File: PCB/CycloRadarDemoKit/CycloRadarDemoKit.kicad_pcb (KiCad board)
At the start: 2 copper layers, 110 x 110 mm, 89 parts, among them J201 ARJM11B1-009-AB-EW2, Q301 L8050QLT1G, Q302 L8050QLT1G, Q401 SI2309CDS, SW101 RESET, SW102 BOOT MODE, U101 ESP32-WROVER-E, U201 IP101GRI, U301 CP2102N-Axx-xQFN28, U401 INA3221, U402 RT8259, U403 TPS2121RUXR, U404 AP63205WU, U405 AP63203WU, Y201 25MHz

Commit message: MPU added, power managemennt updated
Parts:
- removed the C403 at (166.0, 61.5)
- removed the L403 at (162.4, 89.9)
- removed the R402 at (156.3, 62.6)
- removed R418: 0R, Resistor_SMD:R_0805_2012Metric
- added R201: 0R, Resistor_SMD:R_0805_2012Metric, F.Cu at (167.6, 132.5)
- added R308: 5.1K(1%), Resistor_SMD:R_0603_1608Metric, F.Cu at (117.4, 73.5)
- added R309: 5.1K(1%), Resistor_SMD:R_0603_1608Metric, F.Cu at (117.4, 76.0)
- added R414: 47k(1%), Resistor_SMD:R_0603_1608Metric, F.Cu at (172.4, 78.8)
- added U501: MPU-6050, Sensor_Motion:InvenSense_QFN-24_4x4mm_P0.5mm, F.Cu at (160.2, 134.2)
- added U502: LSM6DSM, Package_LGA:LGA-14_3x2.5mm_P0.5mm_LayoutBorder3x4y, F.Cu at (121.8, 50.1)
- added U503: D52MxxM8, RF_Module:Garmin_M8-35_9.8x14.0mm_Layout6x6_P1.5mm, F.Cu at (111.5, 59.8)
- R211: renamed from R210; value 120 -> 270
- R213: renamed from R212; value 100 -> 220
- moved U201 57.6 mm to (105.8, 71.1)
- moved U401 3.49 mm to (188.9, 72.5)
- renumbered C303 to C301, C304 to C302, C301 to C303, C302 to C304, R104 to R107, R105 to R108, R106 to R109, R209 to R210, R213 to R214
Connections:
- net /MAC_TXD(0) renamed /MAC_TXD0
- net /MAC_TXD(1) renamed /MAC_TXD1
- net /USB interface/DTR renamed /USB + LED/DTR
- net /USB interface/RTS renamed /USB + LED/RTS
- net /USB interface/RXD renamed /USB + LED/RXD
- net /USB interface/TXD renamed /USB + LED/TXD
- C401 pad 1: Net-(U401-IN+1) -> Net-(U401-PV)
- C401 pad 2: Net-(U401-IN-1) -> Net-(U401-CRITICAL)
- C402 pad 1: Net-(U401-IN-2) -> Net-(U401-A0)
- C402 pad 2: Net-(U401-IN+2) -> Net-(U401-TC)
- C413 pad 1: /Power management/5V_MUX -> +5V
- D102 pad 3: /IO0 -> /MAC_CLK
- D304 pad 4: /USB interface/LED_DIN -> /LED_DIN
- R109 pad 2: unconnected-(R106-Pad2) -> /GPIO2
- R413 pad 2: +5V -> Net-(D403-A)
- U101 pad 26: unconnected-(U101-ADC2_CH0/GPIO4-Pad26) -> /LED_DIN
- U101 pad 4: unconnected-(U101-SENSOR_VP/GPIO36/ADC1_CH0-Pad4) -> /Photo_res
- U101 pad 5: unconnected-(U101-SENSOR_VN/GPIO39/ADC1_CH3-Pad5) -> /IMU_INT
- U101 pad 6: unconnected-(U101-GPIO34/ADC1_CH6-Pad6) -> SDA
- U101 pad 7: unconnected-(U101-GPIO35/ADC1_CH7-Pad7) -> SCL
- U101 pad 8: unconnected-(U101-32K_XP/GPIO32/ADC1_CH4-Pad8) -> /PMIC_INT
- U101 pad 9: unconnected-(U101-32K_XN/GPIO33/ADC1_CH5-Pad9) -> /12V_DIS
- U401 pad 1: Net-(U401-IN-2) -> GND
- U401 pad 10: /Power management/PMIC_PV -> Net-(U401-PV)
- U401 pad 11: Net-(U401-IN-1) -> unconnected-(U401-IN-1-Pad11)
- U401 pad 12: Net-(U401-IN+1) -> /PMIC_INT
- U401 pad 13: unconnected-(U401-TC-Pad13) -> Net-(U401-TC)
- U401 pad 14: Net-(U401-IN-2) -> unconnected-(U401-IN-2-Pad14)
- U401 pad 15: Net-(U401-IN+2) -> unconnected-(U401-IN+2-Pad15)
- U401 pad 2: unconnected-(U401-IN+3-Pad2) -> SCL
- U401 pad 5: GND -> Net-(U401-A0)
- U401 pad 6: SCL -> unconnected-(U401-SCL-Pad6)
- U401 pad 7: SDA -> unconnected-(U401-SDA-Pad7)
- U401 pad 9: unconnected-(U401-CRITICAL-Pad9) -> Net-(U401-CRITICAL)
- U402 pad 4: /Power management/12V_EN -> /12V_DIS
- U403 pad 1: /Power management/5V_MUX -> +5V
- U403 pad 6: +5V -> Net-(D403-A)
- U403 pad 7: +5V -> Net-(D403-A)
- U403 pad 8: /Power management/5V_MUX -> +5V
- U405 pad 2: /Power management/5V_MUX -> +5V
- U405 pad 3: /Power management/5V_MUX -> +5V

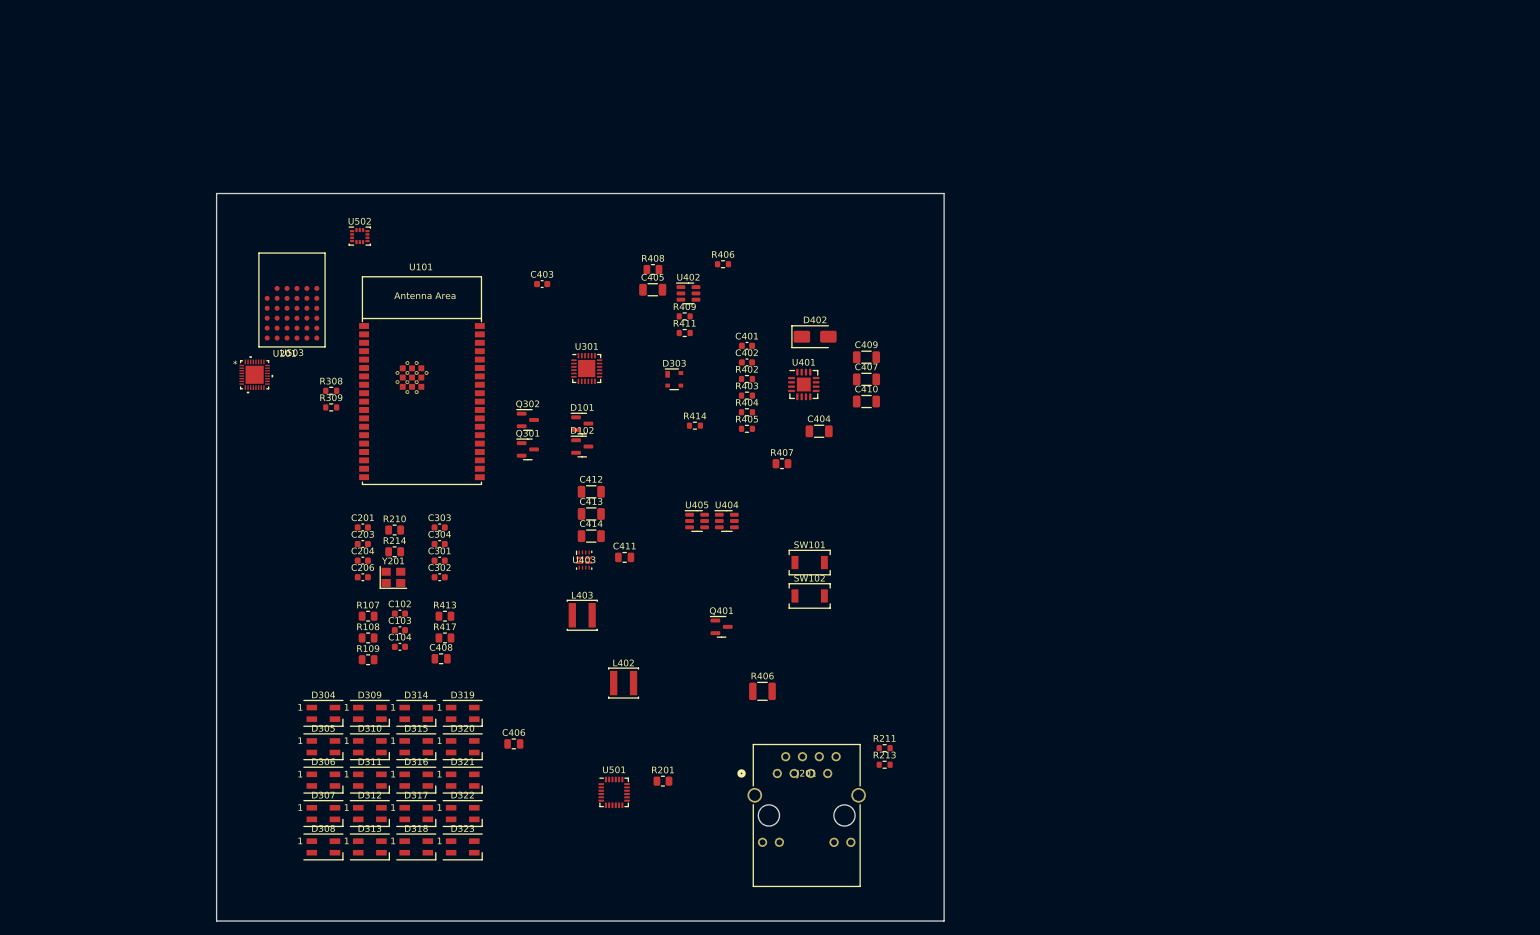
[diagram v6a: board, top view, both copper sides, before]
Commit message: added buzzer and pins for Radar
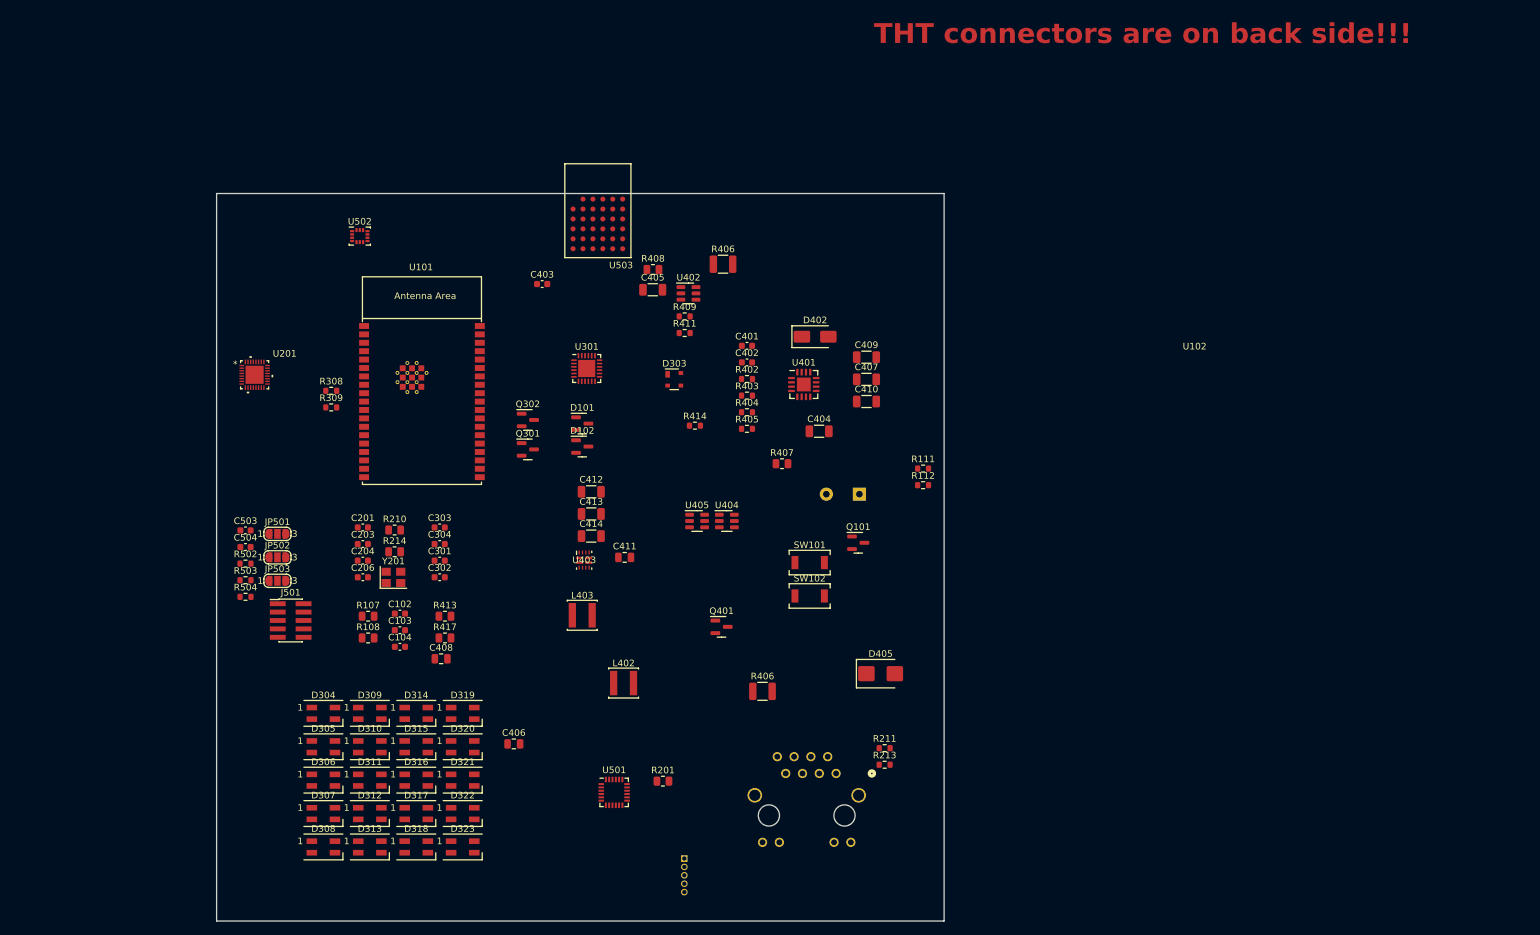
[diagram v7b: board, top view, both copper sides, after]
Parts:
- removed R109: 0R, Resistor_SMD:R_0805_2012Metric
- added BZ101: Buzzer, Buzzer_Beeper:Buzzer_D9mm_P5mm, B.Cu at (197.3, 89.1)
- added C503: 100nF/10V, Capacitor_SMD:C_0603_1608Metric, F.Cu at (104.5, 94.6)
- added C504: 100nF/10V, Capacitor_SMD:C_0603_1608Metric, F.Cu at (104.5, 97.1)
- added D405: SMBJ20A, Diode_SMD:D_SMB, F.Cu at (200.5, 116.2)
- added J101: I2C conn, Connector_PinHeader_1.27mm:PinHeader_1x05_P1.27mm_Vertical, B.Cu at (170.8, 144.2)
- added J501: JTAG, Connector_PinHeader_1.27mm:PinHeader_2x05_P1.27mm_Vertical_SMD, F.Cu at (111.3, 108.2)
- added JP501: BR1, Jumper:SolderJumper-3_P1.3mm_Open_RoundedPad1.0x1.5mm_NumberLabels, F.Cu at (109.3, 95.1)
- added JP502: BR2, Jumper:SolderJumper-3_P1.3mm_Open_RoundedPad1.0x1.5mm_NumberLabels, F.Cu at (109.3, 98.7)
- added JP503: BR3, Jumper:SolderJumper-3_P1.3mm_Open_RoundedPad1.0x1.5mm_NumberLabels, F.Cu at (109.3, 102.2)
- added Q101: L8050QLT1G, Package_TO_SOT_SMD:SOT-23, F.Cu at (197.1, 96.5)
- added R111: ???, Resistor_SMD:R_0603_1608Metric, F.Cu at (206.9, 85.2)
- added R112: 10K(5%), Resistor_SMD:R_0603_1608Metric, F.Cu at (206.9, 87.8)
- added R502: 0R, Resistor_SMD:R_0603_1608Metric, F.Cu at (104.5, 99.6)
- added R503: 0R, Resistor_SMD:R_0603_1608Metric, F.Cu at (104.5, 102.1)
- added R504: 0R, Resistor_SMD:R_0603_1608Metric, F.Cu at (104.5, 104.6)
- added U102: RADAR POGO pins, alps_modules:ALPS Generic Radar 5, F.Cu at (217.5, 100.5)
- J201: moved to B.Cu
- R406: value ??? -> 0.16R(5%); footprint Resistor_SMD:R_0603_1608Metric -> Resistor_SMD:R_1210_3225Metric
- moved U503 48.2 mm to (157.8, 46.2)
- turned J201 to 180 degrees
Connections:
- net Net-(U503-VCC-PadB5) renamed /IMU + ANT/VCC
- C401 pad 1: Net-(U401-PV) -> Net-(U401-IN+1)
- C401 pad 2: Net-(U401-CRITICAL) -> Net-(U401-IN-1)
- C402 pad 1: Net-(U401-A0) -> Net-(U401-IN-2)
- C402 pad 2: Net-(U401-TC) -> Net-(U401-IN+2)
- R406 pad 1: Net-(D402-K) -> Net-(Q401-S)
- R406 pad 2: GND -> Net-(R403-Pad2)
- U101 pad 13: /TMS -> /RXD1
- U101 pad 14: /TDI -> /Radar_GPIO
- U101 pad 16: /TCK -> /RTS1
- U101 pad 23: /TDO -> /TXD1
- U101 pad 24: /GPIO2 -> /Buzzer
- U401 pad 1: GND -> Net-(U401-IN-2)
- U401 pad 10: Net-(U401-PV) -> /PMIC_INT
- U401 pad 11: unconnected-(U401-IN-1-Pad11) -> Net-(U401-IN-1)
- U401 pad 12: /PMIC_INT -> Net-(U401-IN+1)
- U401 pad 13: Net-(U401-TC) -> unconnected-(U401-TC-Pad13)
- U401 pad 14: unconnected-(U401-IN-2-Pad14) -> Net-(U401-IN-2)
- U401 pad 15: unconnected-(U401-IN+2-Pad15) -> Net-(U401-IN+2)
- U401 pad 2: SCL -> unconnected-(U401-IN+3-Pad2)
- U401 pad 5: Net-(U401-A0) -> GND
- U401 pad 6: unconnected-(U401-SCL-Pad6) -> SCL
- U401 pad 7: unconnected-(U401-SDA-Pad7) -> SDA
- U401 pad 9: Net-(U401-CRITICAL) -> unconnected-(U401-CRITICAL-Pad9)
- U503 pad A2: Net-(U503-VSS-PadA2) -> GND
- U503 pad A3: Net-(U503-VSS-PadA2) -> GND
- U503 pad A4: Net-(U503-VSS-PadA2) -> GND
- U503 pad A5: Net-(U503-VSS-PadA2) -> GND
- U503 pad A6: Net-(U503-VSS-PadA2) -> GND
- U503 pad B1: unconnected-(U503-SWDIO-PadB1) -> /IMU + ANT/SWDIO
- U503 pad C1: unconnected-(U503-SWDCLK-PadC1) -> /IMU + ANT/SWDCLK
- U503 pad D1: unconnected-(U503-P008-PadD1) -> /TXD1
- U503 pad D2: unconnected-(U503-P014-PadD2) -> /RXD1
- U503 pad D4: unconnected-(U503-P022-PadD4) -> Net-(U503-P022)
- U503 pad D6: unconnected-(U503-P024-PadD6) -> /IMU + ANT/BR2
- U503 pad E1: unconnected-(U503-P006-PadE1) -> /IMU + ANT/BR3
- U503 pad E3: unconnected-(U503-AIN1/P003-PadE3) -> /IMU + ANT/BR1
- U503 pad E5: unconnected-(U503-AIN0/P002-PadE5) -> GND
- U503 pad E6: unconnected-(U503-P021/RESET-PadE6) -> /EN
- U503 pad F1: unconnected-(U503-P025-PadF1) -> Net-(U503-P025)
- U503 pad F2: unconnected-(U503-AIN7/P031-PadF2) -> /RTS1
- U503 pad F5: unconnected-(U503-AIN4/P028-PadF5) -> Net-(U503-AIN4/P028)
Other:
- copper layers 2 -> 4
- board text added: "THT connectors are on back side!!!"

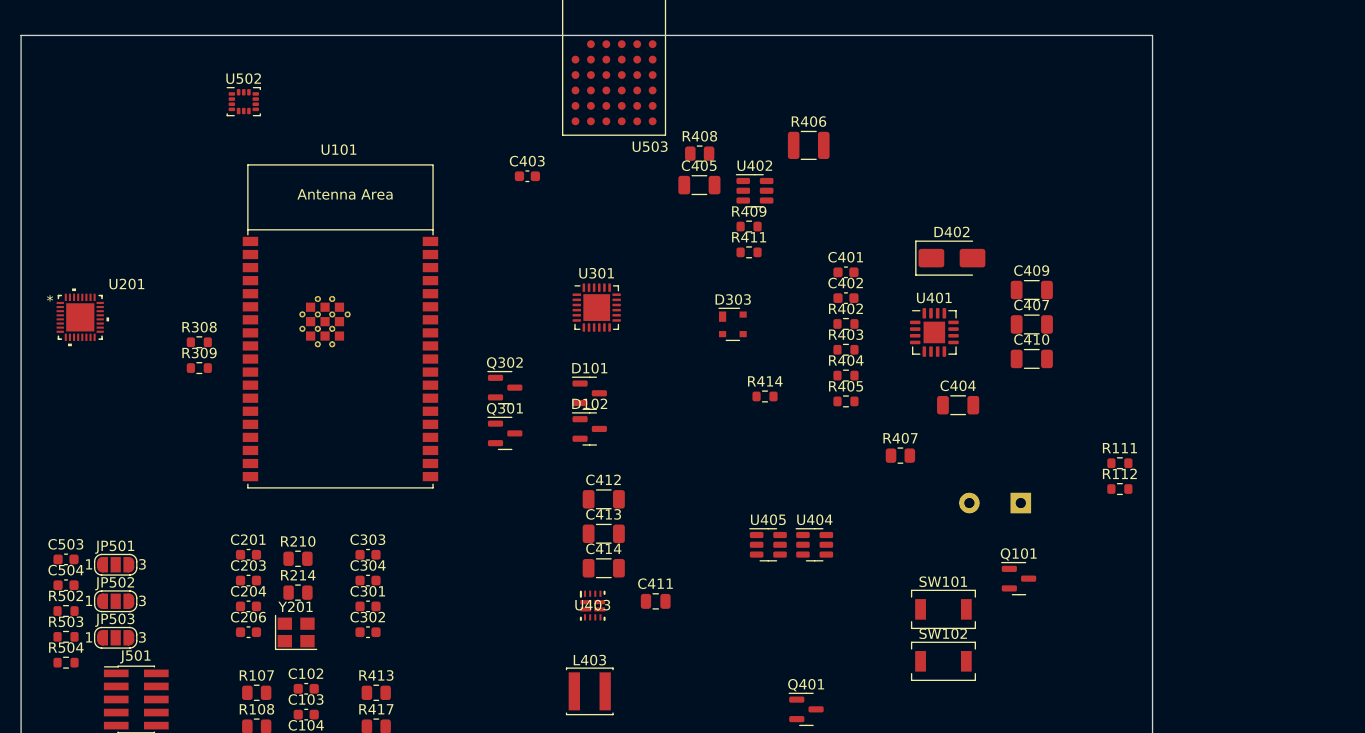
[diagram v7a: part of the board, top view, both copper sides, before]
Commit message: more components fthprnt added
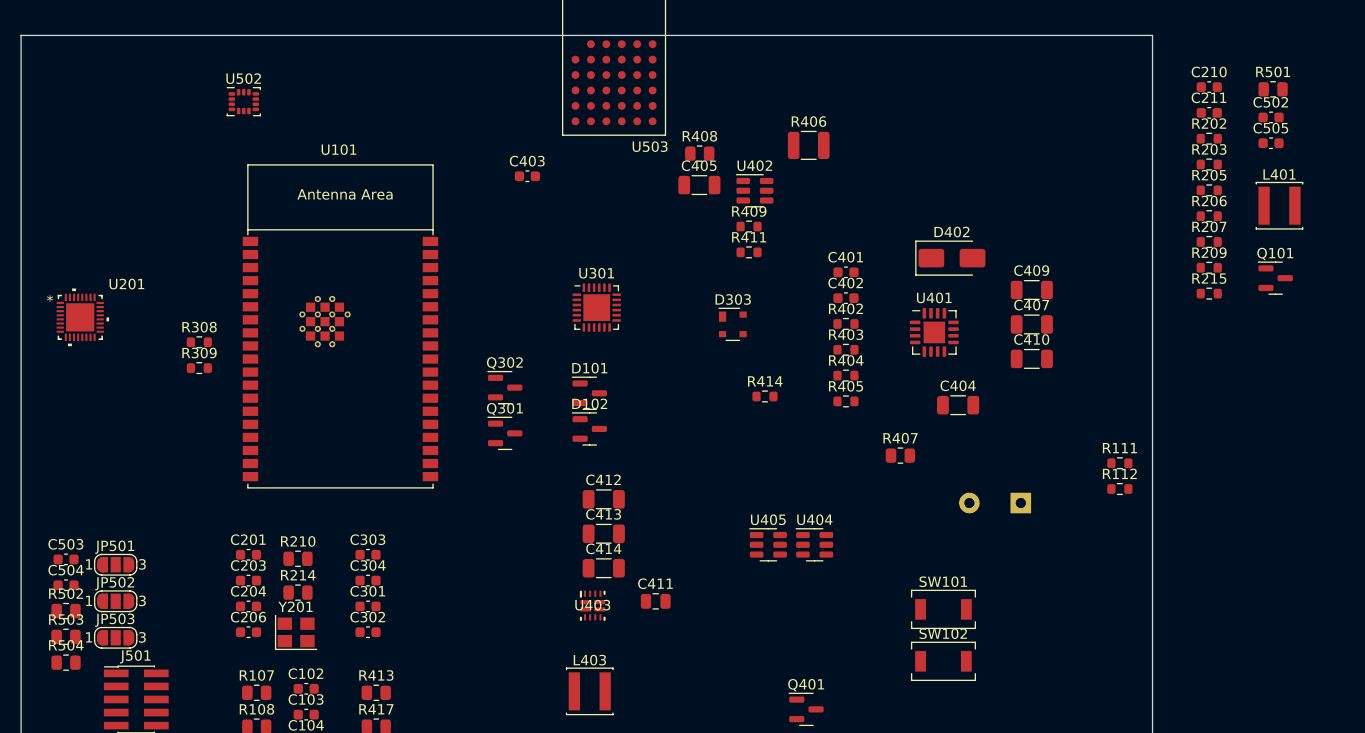
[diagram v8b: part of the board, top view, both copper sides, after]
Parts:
- added C210: 0.1uF/50V(10%), Capacitor_SMD:C_0603_1608Metric, F.Cu at (215.6, 48.7)
- added C211: 0.1uF/50V(10%), Capacitor_SMD:C_0603_1608Metric, F.Cu at (215.6, 51.2)
- added C502: 0.1uF/50V(10%), Capacitor_SMD:C_0603_1608Metric, F.Cu at (221.6, 51.6)
- added C505: 0.1uF/50V(10%), Capacitor_SMD:C_0603_1608Metric, F.Cu at (221.6, 54.1)
- added L401: 15uH/1A, Inductor_SMD:L_Changjiang_FNR4018S, F.Cu at (222.4, 60.2)
- added R202: 5.1K(1%), Resistor_SMD:R_0603_1608Metric, F.Cu at (215.6, 53.7)
- added R203: 5.1K(1%), Resistor_SMD:R_0603_1608Metric, F.Cu at (215.6, 56.2)
- added R205: 5.1K(1%), Resistor_SMD:R_0603_1608Metric, F.Cu at (215.6, 58.7)
- added R206: 5.1K(1%), Resistor_SMD:R_0603_1608Metric, F.Cu at (215.6, 61.2)
- added R207: 5.1K(1%), Resistor_SMD:R_0603_1608Metric, F.Cu at (215.6, 63.7)
- added R209: 5.1K(1%), Resistor_SMD:R_0603_1608Metric, F.Cu at (215.6, 66.2)
- added R215: 5.1K(1%), Resistor_SMD:R_0603_1608Metric, F.Cu at (215.6, 68.8)
- added R501: 0R, Resistor_SMD:R_0805_2012Metric, F.Cu at (221.8, 48.9)
- R502, R503, R504: footprint Resistor_SMD:R_0603_1608Metric -> Resistor_SMD:R_0805_2012Metric
- moved Q101 38.4 mm to (222.1, 67.2)
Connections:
- Q101 pad 2: Net-(BZ101-+) -> GND
- Q101 pad 3: GND -> Net-(BZ101-+)
